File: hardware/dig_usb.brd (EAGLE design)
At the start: 146.1 x 102.6 mm, 172 parts, among them IC1 AT90USB1287-AU, IC202 DS1337S, IC203 MAX487CSA, IC204 74HC166D, IC301 LTV-356T, IC302 LTV-356T, IC303 LTV-356T, IC304 LTV-356T, IC305 LTV-356T, IC306 LTV-356T, IC307 LTV-356T, IC308 LTV-356T, K401 S202S02, K402 S202S02, K403 S202S02, K404 S202S02, K405 S202S02, K406 S202S02, K407 S202S02, K408 S202S02, Q1 16MHz, Q201 32,768kHz, T301 BCR191, T302 BCR191, T303 BCR191, T304 BCR191, T305 BCR191, T306 BCR191, T307 BCR191, T308 BCR191, X101 RIA-73-02, X201 ISP, X202 RIA-73-02, X301 RIA-73-02, X302 RIA-73-02, X303 RIA-73-02, X304 RIA-73-02, X305 RIA-73-02, X401 RIA-73-02, X402 RIA-73-02, X403 RIA-73-02, X404 RIA-73-02, X405 RIA-73-02

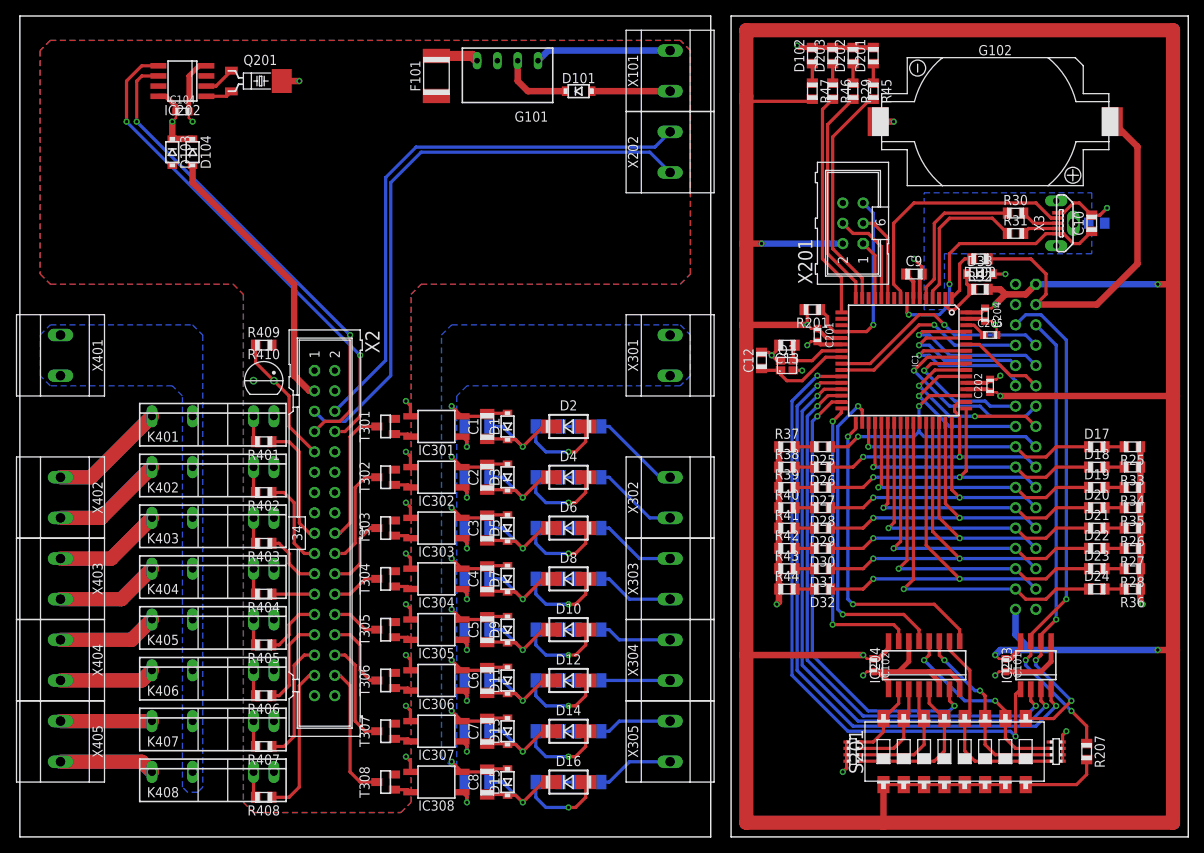
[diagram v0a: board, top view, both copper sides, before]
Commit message: Unterer Wannenstecker auf dig_usb verschoben um Platz für Wärmebrücke zu machen
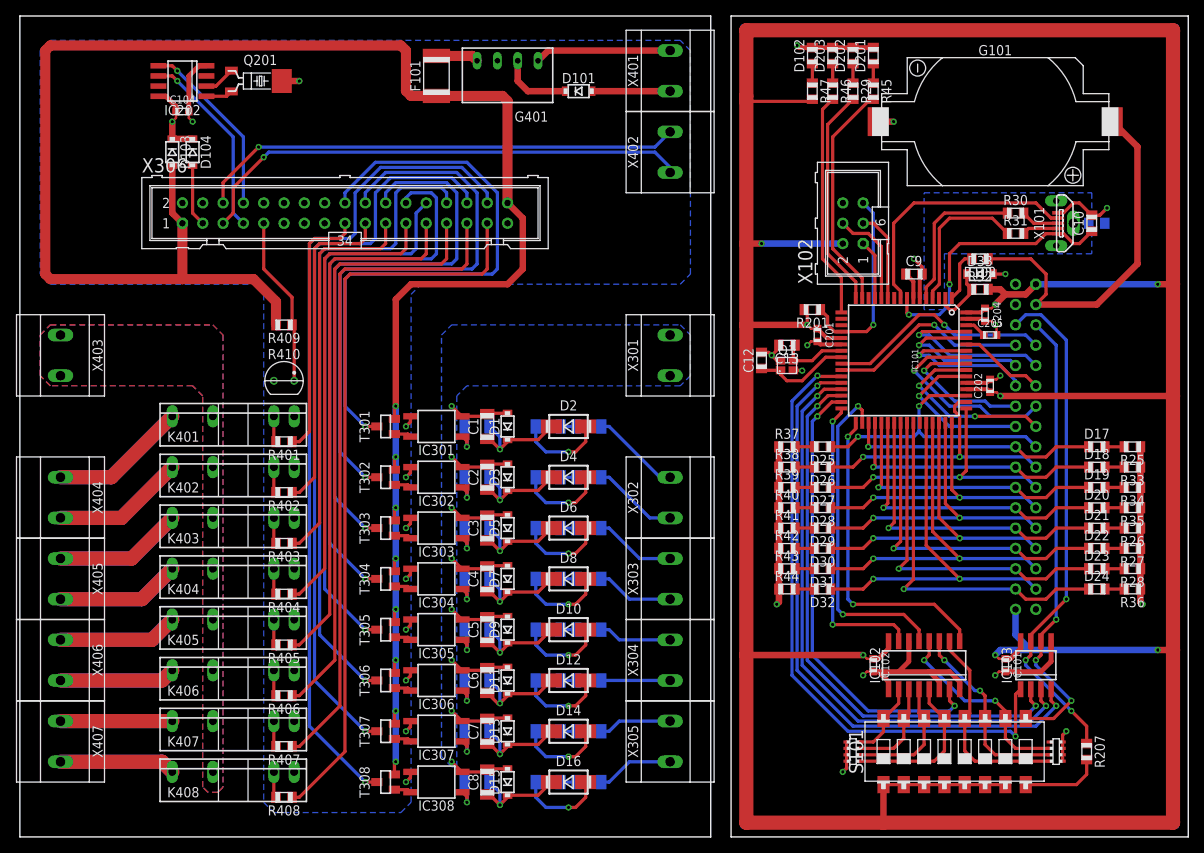
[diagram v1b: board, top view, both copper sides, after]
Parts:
- removed G102: KZH20SMD-2, batterie:KHZ20SMD-2
- removed X2: (no value), anschluss:WS34V
- removed X202: RIA-73-02, anschluss:RIA-73-02
- removed X3: (no value), stecker:MOLEX_1051330011
- added G401: TME2405S, schaltregler:TME-24V
- added X306: (no value), anschluss:WS34V
- added X406, X407: RIA-73-02, anschluss:RIA-73-02
- G101: value TME2405S -> KZH20SMD-2; device schaltregler:TME-24V -> batterie:KHZ20SMD-2
- X101: value RIA-73-02 -> (none); device anschluss:RIA-73-02 -> stecker:MOLEX_1051330011
- moved X402 87.6 mm to (81.3, 85.1), turned to 90 degrees
- moved X401 84.1 mm to (81.3, 95.2), turned to 90 degrees
- moved G101 61.4 mm to (121.9, 88.9), turned to 0 degrees
- moved X101 51.9 mm to (129.5, 76.2)
- moved X403 27.9 mm to (5.08, 59.7)
- moved X405 20.3 mm to (5.08, 31.8)
- moved X404 20.3 mm to (5.08, 41.9)
- moved R409 3.59 mm to (33.0, 63.5), turned to 180 degrees
- moved K401 2.54 mm to (26.7, 52.1)
- moved K402 2.54 mm to (26.7, 45.7)
- moved K403 2.54 mm to (26.7, 39.4)
- moved K404 2.54 mm to (26.7, 33.0)
- moved K405 2.54 mm to (26.7, 26.7)
- moved K406 2.54 mm to (26.7, 20.3)
- moved K407 2.54 mm to (26.7, 14.0)
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- renumbered IC1 to IC101, IC203 to IC103, IC204 to IC102, S201 to S101, X201 to X102, X4 to X103
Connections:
- net +5V: now also X306.1, X306.34; no longer X2.1, X2.34
- net GND: now also G101.-, G401.3, X101.5, X306.2, X306.33, X306.4; no longer G101.3, G102.-, X2.2, X2.33, X2.4, X3.5
- net L: now also X403.1, X403.2; no longer X401.1, X401.2
- net N$100: now also X306.30; no longer X2.30
- net N$101: now also X306.32; no longer X2.32
- net N$119: now also X101.3; no longer X3.3
- net N$121: now also X101.2; no longer X3.2
- net N$123: now also X101.4; no longer X3.4
- net N$124: now also X101.1; no longer X3.1
- net N$130: now also X306.3; no longer X2.3
- net N$131: now also X306.7; no longer X2.7
- net N$132: now also X306.8; no longer X2.8
- net N$133: now also X306.6, X402.2; no longer X2.6, X202.2
- net N$134: now also X306.5, X402.1; no longer X2.5, X202.1
- net N$143: now also G101.+; no longer G102.+
- net N$146: now also X306.9; no longer X2.9
- net N$19: now also G401.1, X401.2; no longer G101.1, X101.2
- net N$23: now also G401.2; no longer G101.2
- net N$24: now also X401.1; no longer X101.1
- net N$41: now also G401.4; no longer G101.4
- net N$67: now also X306.17; no longer X2.17
- net N$68: now also X404.1; no longer X402.1
- net N$72: now also X404.2; no longer X402.2
- net N$74: now also X405.1; no longer X403.1
- net N$76: now also X405.2; no longer X403.2
- net N$78: now also X406.1; no longer X404.1
- net N$79: now also X306.19; no longer X2.19
- net N$82: now also X406.2; no longer X404.2
- net N$84: now also X407.1; no longer X405.1
- net N$87: now also X306.21; no longer X2.21
- net N$88: now also X306.23; no longer X2.23
- net N$89: now also X407.2; no longer X405.2
- net N$90: now also X306.25; no longer X2.25
- net N$91: now also X306.27; no longer X2.27
- net N$92: now also X306.29; no longer X2.29
- net N$93: now also X306.31; no longer X2.31
- net N$94: now also X306.18; no longer X2.18
- net N$95: now also X306.20; no longer X2.20
- net N$96: now also X306.22; no longer X2.22
- net N$97: now also X306.24; no longer X2.24
- net N$98: now also X306.26; no longer X2.26
- net N$99: now also X306.28; no longer X2.28
- net USHIELD: now also X101.S1, X101.S2, X101.S3; no longer X3.S1, X3.S2, X3.S3
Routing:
- net +5V: track 469.1 -> 719.1 mm, vias 8 -> 16
- net N$101: track 17.1 -> 103.4 mm, vias 0 -> 1
- net N$100: track 13.3 -> 92.5 mm, vias 0 -> 1
- net N$93: track 19.1 -> 92.1 mm
- net N$99: track 9.48 -> 81.7 mm, vias 0 -> 1
- net N$92: track 15.3 -> 83.5 mm
- net N$91: track 11.5 -> 75.0 mm
- net N$97: track 6.04 -> 68.5 mm, vias 0 -> 1
- net N$98: track 6.04 -> 68.1 mm, vias 0 -> 1
- net N$96: track 9.48 -> 70.6 mm, vias 0 -> 1
- net N$90: track 7.67 -> 66.5 mm
- net N$95: track 13.3 -> 72.1 mm, vias 0 -> 1
- net N$94: track 17.1 -> 73.5 mm, vias 0 -> 1
- net N$88: track 5.35 -> 58.0 mm
- net N$87: track 7.67 -> 49.5 mm
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- added copper zone on layer 1, net L
- removed copper zone on layer 1, net +5V

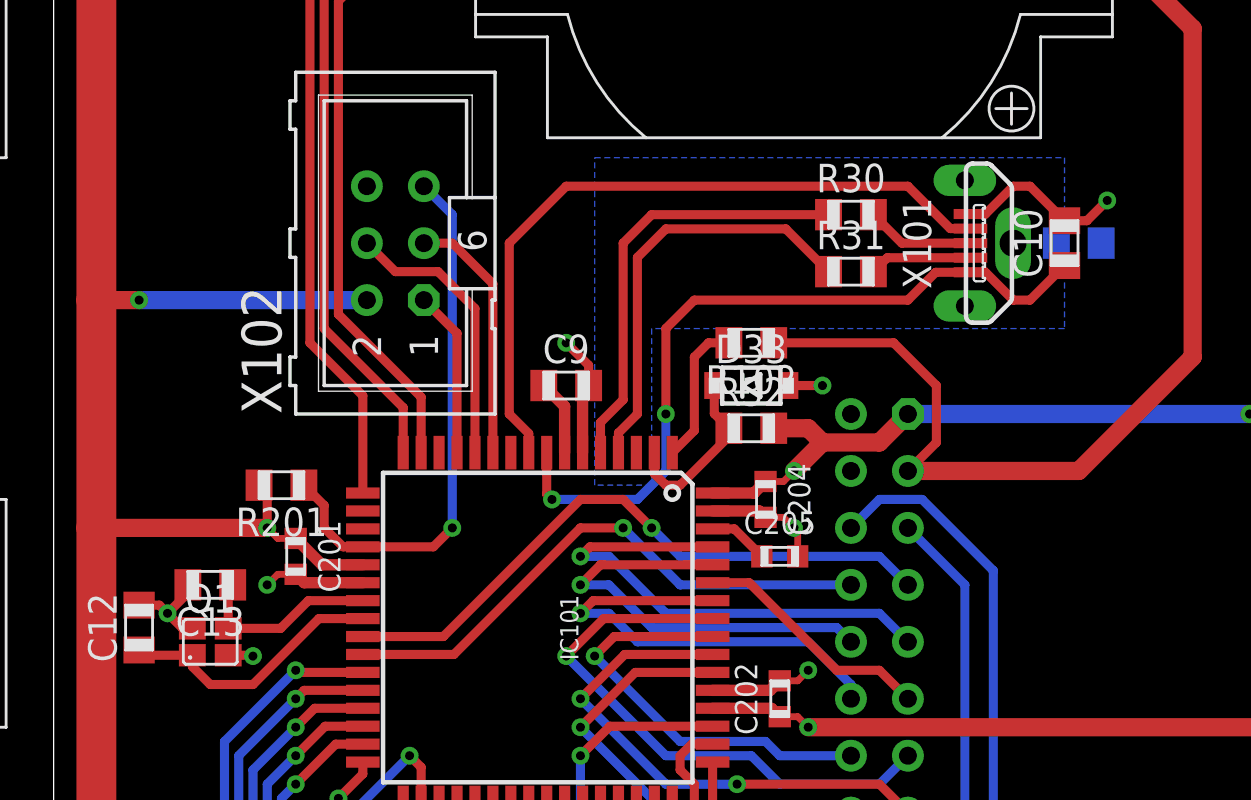
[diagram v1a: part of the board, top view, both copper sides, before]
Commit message: USB Buchse ausgetauscht
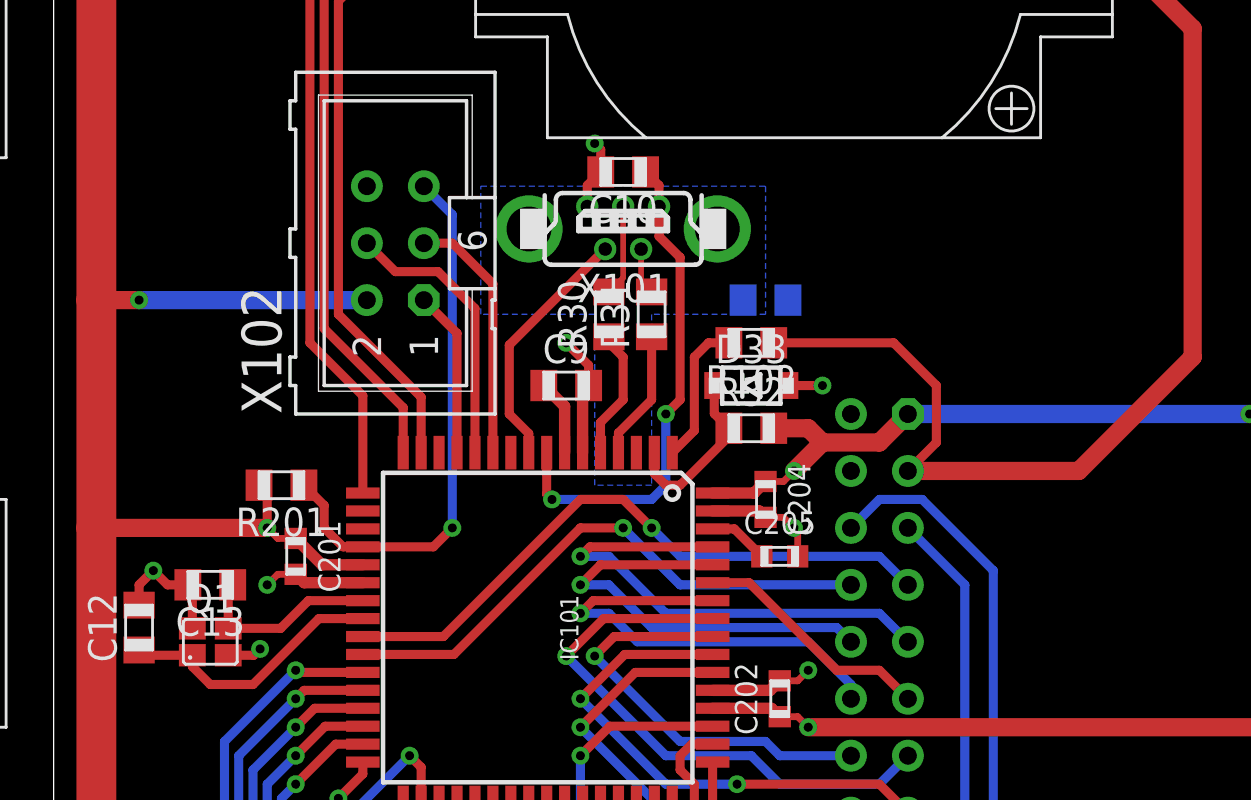
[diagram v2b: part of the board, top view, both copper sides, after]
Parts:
- X101: device stecker:MOLEX_1051330011 -> stecker:WE651005136421
- moved C10 19.9 mm to (114.3, 79.4), turned to 180 degrees
- moved X101 15.3 mm to (114.3, 76.8), turned to 180 degrees
- moved C11 14.2 mm to (120.7, 73.7)
- moved R30 11.7 mm to (113.7, 73.0), turned to 90 degrees
- moved R31 9.09 mm to (115.6, 73.0), turned to 90 degrees
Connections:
- net USHIELD: no longer X101.S3
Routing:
- net N$123: track 32.1 -> 11.2 mm
- net N$120: track 19.4 -> 5.85 mm
- net N$122: track 18.9 -> 5.78 mm
- net N$124: track 34.1 -> 22.4 mm
- net GND: track 150.6 -> 147.4 mm
- net N$121: track 4.59 -> 2.10 mm
- net N$119: track 4.86 -> 4.07 mm

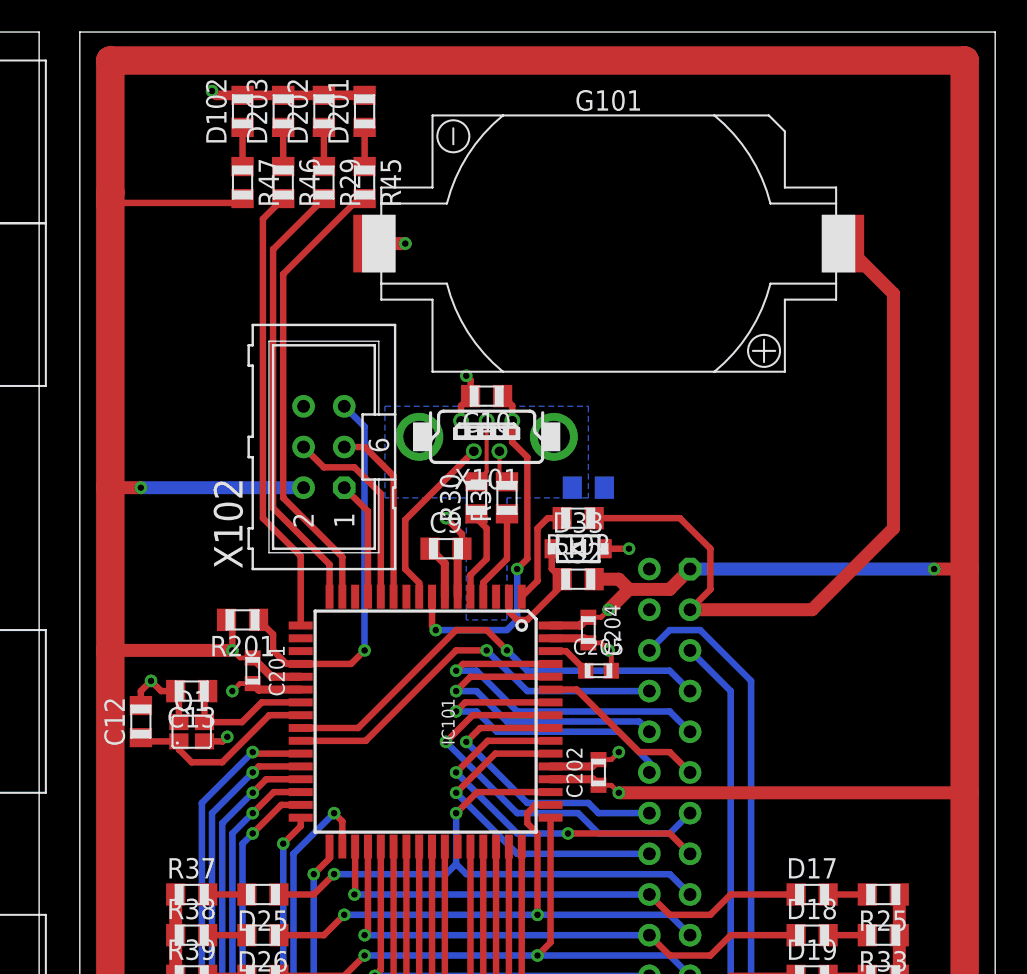
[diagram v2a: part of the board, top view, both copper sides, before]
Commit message: UVCC und HWB angeschlossen
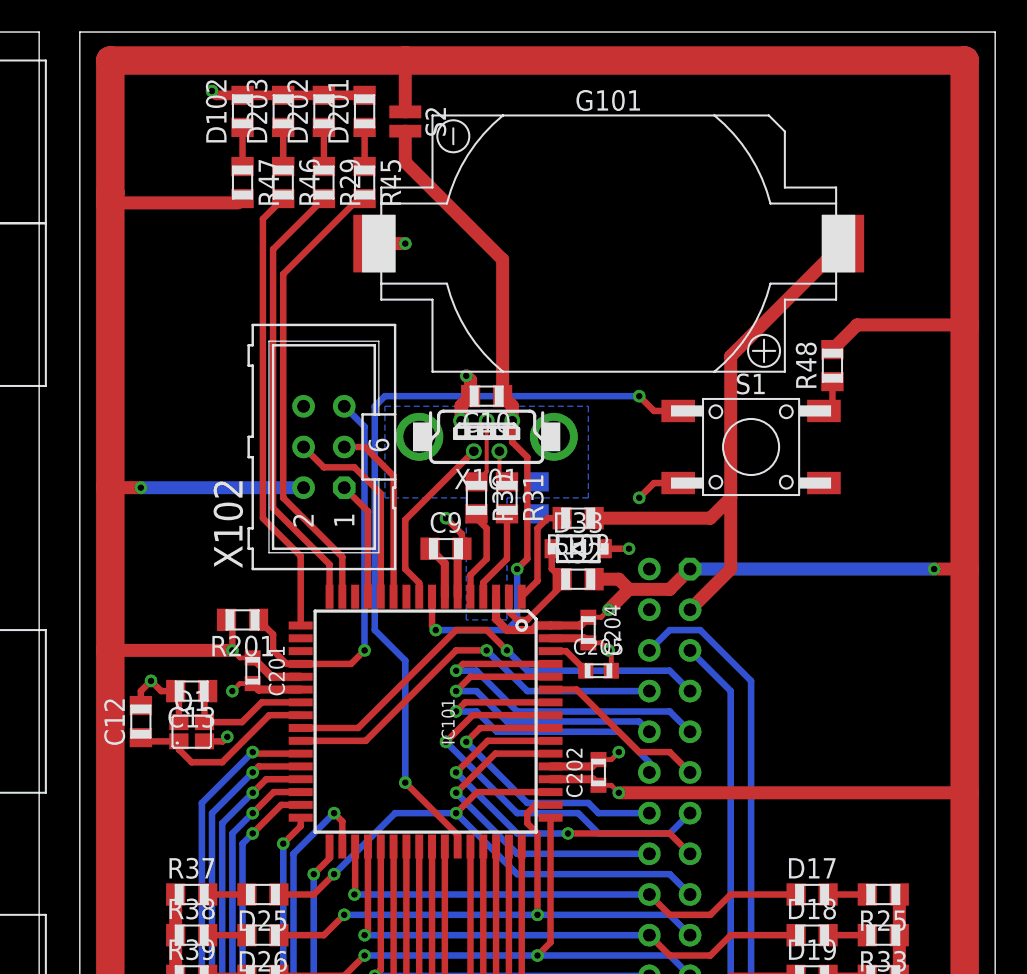
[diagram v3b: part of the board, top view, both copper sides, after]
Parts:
- added R48: 10kΩ, passiv:CHIP_0805
- added S1: (no value), schalter:SCHURTER1301
- added S2: (no value), schalter:JUMPER2
- moved C11 3.24 mm to (117.5, 73.0), turned to 270 degrees
- turned R30 to 270 degrees
- turned R31 to 270 degrees
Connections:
- removed net UVCC: IC101.3
- new net N$147: IC101.43, R48.1, S1.3, S1.4
- net +5V: now also IC101.3, R48.2, S2.P$1
- net GND: now also S1.1, S1.2
- net N$119: now also R30.1; no longer R30.2
- net N$120: now also R30.2; no longer R30.1
- net N$121: now also R31.1; no longer R31.2
- net N$122: now also R31.2; no longer R31.1
- net N$124: now also S2.P$2
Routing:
- net N$147: track 0.00 -> 51.3 mm, vias 0 -> 2
- net N$124: track 22.4 -> 41.5 mm
- net +5V: track 719.1 -> 736.5 mm
- net N$143: track 46.3 -> 35.9 mm
- net GND: track 147.4 -> 150.3 mm, vias 26 -> 27
- net OUT0: track 36.9 -> 36.3 mm
